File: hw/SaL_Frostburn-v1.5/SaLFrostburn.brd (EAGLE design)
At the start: 72.6 x 19.7 mm, 100 parts, among them U1 ATSAMD21G-A, U2 CC1120, U3 ADXL345, U4 gps, Y1 32.768kHx, Y3 32MHz

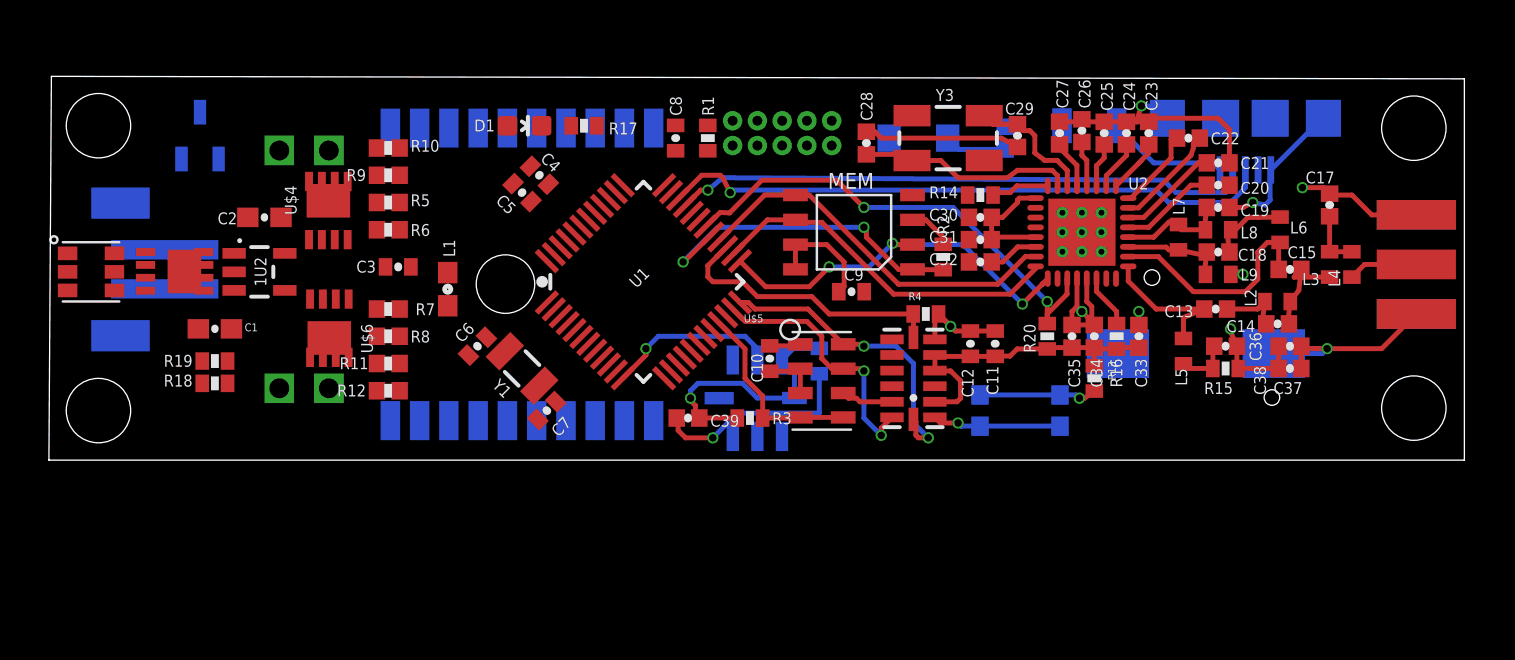
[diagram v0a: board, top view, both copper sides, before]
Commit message: SaLFrostburn-v1.1 hw finished and ordered
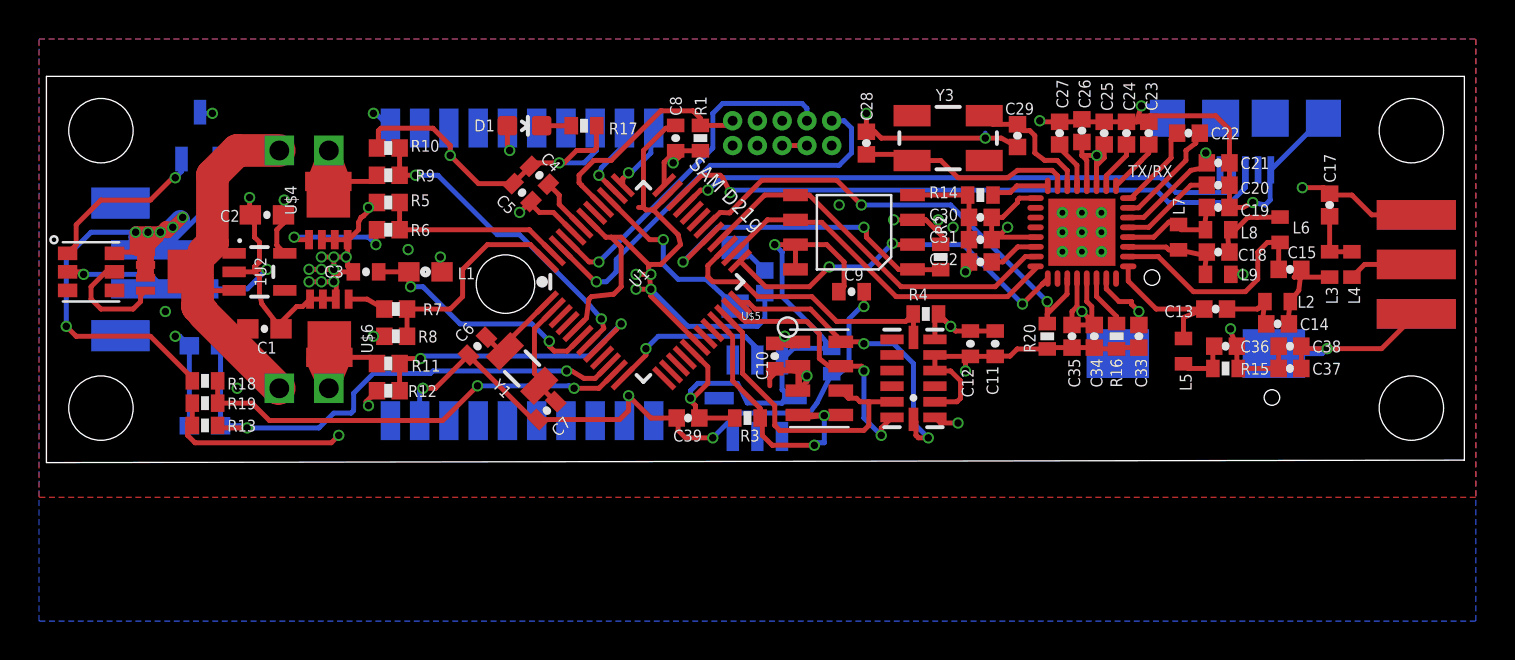
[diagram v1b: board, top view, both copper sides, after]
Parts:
- removed F1: PTCSMD, SparkFun-PowerIC:PTC-1206
- moved R13 45.7 mm to (3.43, 1.78), turned to 0 degrees
- moved S2 41.8 mm to (3.43, 3.81), turned to 270 degrees
- moved R21 14.4 mm to (32.1, 9.14), turned to 270 degrees
- moved D2 11.8 mm to (30.6, 9.40), turned to 90 degrees
- moved C1 2.54 mm to (6.48, 6.73)
- moved R19 2.22 mm to (3.43, 2.92), turned to 0 degrees
- moved C3 1.67 mm to (11.7, 9.65)
- moved L1 1.45 mm to (14.7, 9.65), turned to 180 degrees
- moved C16 0.64 mm to (35.6, 5.08)
- moved R18 0.52 mm to (3.43, 4.06), turned to 180 degrees
- moved R1 0.38 mm to (28.8, 16.5)
- moved R7 0.38 mm to (13.2, 7.75)
- moved R8 0.38 mm to (13.2, 6.35)
- moved C10 0.28 mm to (32.6, 5.33)
- moved STANDOFF2 0.28 mm to (-1.91, 16.9)
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- renumbered U2 to TX/RX
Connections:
- removed net N$14: F1.1, JP4.VBUS
- net GND: now also U$4.1, U$4.2, U$4.3, U$6.1, U$6.2, U$6.3
- net LVD_IN: no longer F1.2
- net PROG: now also U1.10; no longer U1.11
- net SENSE_BAT: now also U1.11; no longer U1.10
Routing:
- net GND: track 92.7 -> 335.5 mm, vias 6 -> 43
- net 3.3V: track 77.7 -> 201.0 mm, vias 6 -> 19
- net RAW: track 0.00 -> 39.8 mm, vias 0 -> 6
- net LVD_IN: track 0.00 -> 26.2 mm
- net SENSE_BAT: track 0.00 -> 23.1 mm, vias 0 -> 2
- net PROG: track 6.05 -> 27.7 mm, vias 1 -> 2
- net SWDIO: track 0.00 -> 21.2 mm, vias 0 -> 1
- net SWCLK: track 0.00 -> 17.9 mm, vias 0 -> 1
- net SENSE_A: track 0.00 -> 16.5 mm, vias 0 -> 2
- net SENSE_B: track 0.00 -> 15.6 mm, vias 0 -> 2
- net SPI2_MISO: track 2.68 -> 15.7 mm
- net N$5: track 0.00 -> 12.9 mm, vias 0 -> 2
- net !RESET: track 0.00 -> 11.9 mm
- net FET_A: track 0.00 -> 11.9 mm
- net FET_B: track 0.00 -> 11.3 mm
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- added copper zone on layer 15, net 3.3V
- added copper zone on layer 1, net GND
- added copper zone on layer 16, net GND
- added copper zone on layer 2, net GND
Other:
- board size 72.6 x 19.7 mm -> 72.7 x 19.8 mm
- board text added: "SAM D21g"
- board text added: "SaLFrostburn V1.1"
